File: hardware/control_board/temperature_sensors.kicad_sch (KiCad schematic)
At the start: 23 parts, among them J5 RTD, J5 TC, U2 MAX6675, U6 MCP6N11T-005E, U7 MCP6001T

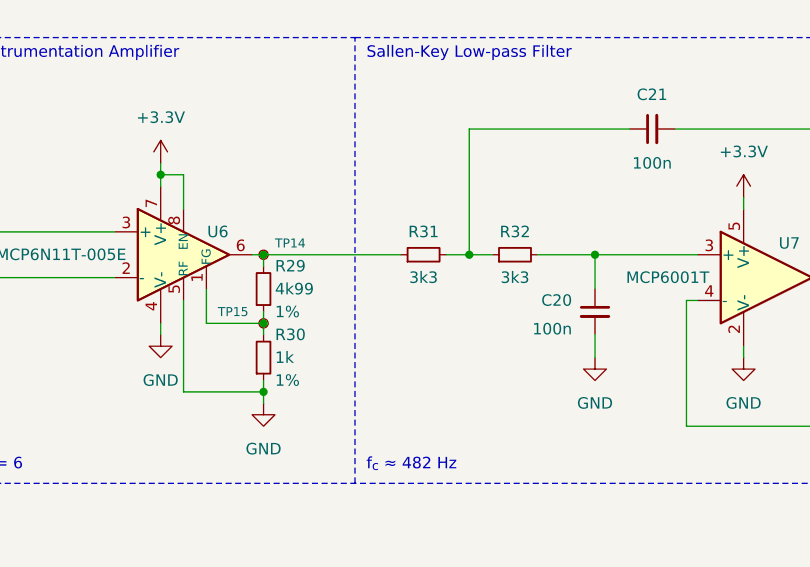
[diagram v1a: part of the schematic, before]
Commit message: Change the buzzer
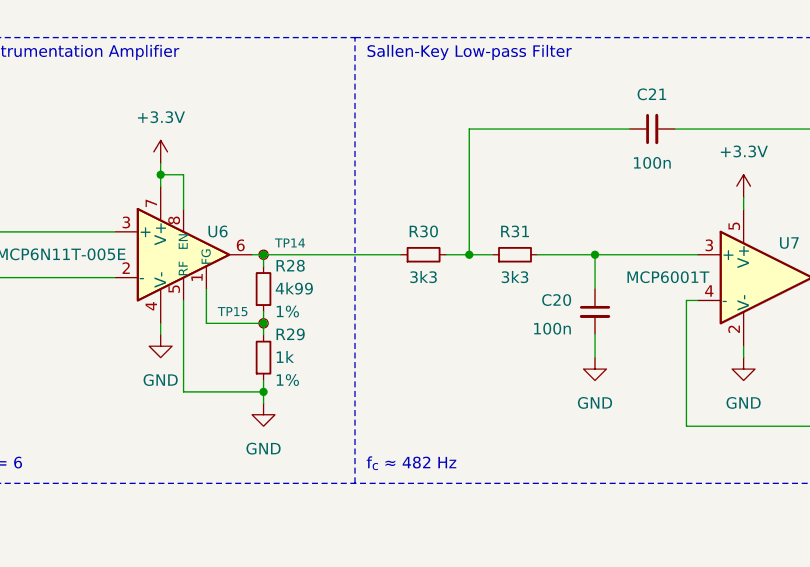
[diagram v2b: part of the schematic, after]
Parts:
- renumbered R29 to R28, R30 to R29, R31 to R30, R32 to R31
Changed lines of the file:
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@@
       (project "control_board"
         (path "/b652b05a-4e3d-4ad1-b032-18886abe7d45/02711725-e382-48ba-bf33-23fe46c66e66"
-          (reference "R28") (unit 1)
+          (reference "R27") (unit 1)
         )
       )
@@
       (project "control_board"
         (path "/b652b05a-4e3d-4ad1-b032-18886abe7d45/02711725-e382-48ba-bf33-23fe46c66e66"
-          (reference "R26") (unit 1)
+          (reference "R25") (unit 1)
         )
       )
@@
       (project "control_board"
         (path "/b652b05a-4e3d-4ad1-b032-18886abe7d45/02711725-e382-48ba-bf33-23fe46c66e66"
-          (reference "R27") (unit 1)
+          (reference "R26") (unit 1)
         )
       )
@@
   (symbol (lib_id "Device:R_Small") (at 146.05 62.23 0) (mirror x) (unit 1)
     (in_bom yes) (on_board yes) (dnp no)
-    (property "Reference" "R29" (at 147.32 59.69 0)
+    (property "Reference" "R28" (at 147.32 59.69 0)
       (effects (font (size 1.27 1.27)) (justify left))
     )
@@
       (project "control_board"
         (path "/b652b05a-4e3d-4ad1-b032-18886abe7d45/02711725-e382-48ba-bf33-23fe46c66e66"
-          (reference "R29") (unit 1)
+          (reference "R28") (unit 1)
         )
       )
@@
   (symbol (lib_id "Device:R_Small") (at 173.99 58.42 90) (unit 1)
     (in_bom yes) (on_board yes) (dnp no)
-    (property "Reference" "R32" (at 173.99 55.88 90)
+    (property "Reference" "R31" (at 173.99 55.88 90)
       (effects (font (size 1.27 1.27)))
     )
@@
       (project "control_board"
         (path "/b652b05a-4e3d-4ad1-b032-18886abe7d45/02711725-e382-48ba-bf33-23fe46c66e66"
-          (reference "R32") (unit 1)
+          (reference "R31") (unit 1)
         )
       )
@@
   (symbol (lib_id "Device:R_Small") (at 146.05 69.85 0) (mirror x) (unit 1)
     (in_bom yes) (on_board yes) (dnp no)
-    (property "Reference" "R30" (at 147.32 67.31 0)
+    (property "Reference" "R29" (at 147.32 67.31 0)
       (effects (font (size 1.27 1.27)) (justify left))
     )
@@
       (project "control_board"
         (path "/b652b05a-4e3d-4ad1-b032-18886abe7d45/02711725-e382-48ba-bf33-23fe46c66e66"
+          (reference "R29") (unit 1)
+        )
+      )
+      (project "apps"
+        (path "/fc4ad874-c922-4070-89f9-7262080469d8/00000000-0000-0000-0000-00006068dc5c"
+          (reference "R?") (unit 1)
+        )
+      )
+    )
+  )
+  (symbol (lib_id "Device:R_Small") (at 163.83 58.42 90) (unit 1)
+    (in_bom yes) (on_board yes) (dnp no)
+    (property "Reference" "R30" (at 163.83 55.88 90)
+      (effects (font (size 1.27 1.27)))
+    )
+    (property "Value" "3k3" (at 163.83 60.96 90)
+      (effects (font (size 1.27 1.27)))
+    )
+    (property "Footprint" "Resistor_SMD:R_0603_1608Metric" (at 163.83 58.42 0)
+      (effects (font (size 1.27 1.27)) hide)
+    )
+    (property "Datasheet" "~" (at 163.83 58.42 0)
+      (effects (font (size 1.27 1.27)) hide)
+    )
+    (pin "1")
+    (pin "2")
+    (instances
+      (project "control_board"
+        (path "/b652b05a-4e3d-4ad1-b032-18886abe7d45/02711725-e382-48ba-bf33-23fe46c66e66"
           (reference "R30") (unit 1)
         )
       )
-      (project "apps"
-        (path "/fc4ad874-c922-4070-89f9-7262080469d8/00000000-0000-0000-0000-00006068dc5c"
-          (reference "R?") (unit 1)
-        )
-      )
-    )
-  )
-  (symbol (lib_id "Device:R_Small") (at 163.83 58.42 90) (unit 1)
-    (in_bom yes) (on_board yes) (dnp no)
-    (property "Reference" "R31" (at 163.83 55.88 90)
-      (effects (font (size 1.27 1.27)))
-    )
-    (property "Value" "3k3" (at 163.83 60.96 90)
-      (effects (font (size 1.27 1.27)))
-    )
-    (property "Footprint" "Resistor_SMD:R_0603_1608Metric" (at 163.83 58.42 0)
-      (effects (font (size 1.27 1.27)) hide)
-    )
-    (property "Datasheet" "~" (at 163.83 58.42 0)
-      (effects (font (size 1.27 1.27)) hide)
-    )
-    (pin "1")
-    (pin "2")
-    (instances
-      (project "control_board"
-        (path "/b652b05a-4e3d-4ad1-b032-18886abe7d45/02711725-e382-48ba-bf33-23fe46c66e66"
-          (reference "R31") (unit 1)
-        )
-      )

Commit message: Add USB D+ pull-up resistor
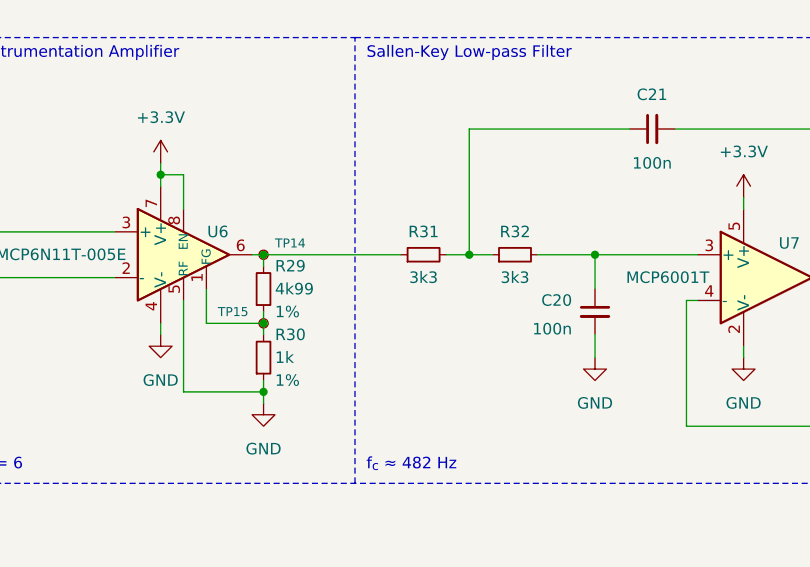
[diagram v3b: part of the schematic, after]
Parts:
- renumbered R28 to R29, R29 to R30, R30 to R31, R31 to R32
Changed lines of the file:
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@@
         )
         (path "/b652b05a-4e3d-4ad1-b032-18886abe7d45/02711725-e382-48ba-bf33-23fe46c66e66"
-          (reference "#PWR064") (unit 1)
+          (reference "#PWR065") (unit 1)
         )
         (path "/b652b05a-4e3d-4ad1-b032-18886abe7d45/d341d3a2-ea4e-4772-851c-7c5b5be32855"
@@
   (symbol (lib_id "power:GND") (at 182.88 69.85 0) (unit 1)
     (in_bom yes) (on_board yes) (dnp no)
-    (property "Reference" "#PWR071" (at 182.88 76.2 0)
+    (property "Reference" "#PWR072" (at 182.88 76.2 0)
       (effects (font (size 1.27 1.27)) hide)
     )
@@
       (project "control_board"
         (path "/b652b05a-4e3d-4ad1-b032-18886abe7d45/02711725-e382-48ba-bf33-23fe46c66e66"
-          (reference "#PWR071") (unit 1)
+          (reference "#PWR072") (unit 1)
         )
       )
@@
       (project "control_board"
         (path "/b652b05a-4e3d-4ad1-b032-18886abe7d45/02711725-e382-48ba-bf33-23fe46c66e66"
-          (reference "R27") (unit 1)
+          (reference "R28") (unit 1)
         )
       )
@@
       (project "control_board"
         (path "/b652b05a-4e3d-4ad1-b032-18886abe7d45/02711725-e382-48ba-bf33-23fe46c66e66"
-          (reference "R25") (unit 1)
+          (reference "R26") (unit 1)
         )
       )
@@
         )
         (path "/b652b05a-4e3d-4ad1-b032-18886abe7d45/02711725-e382-48ba-bf33-23fe46c66e66"
-          (reference "#PWR063") (unit 1)
+          (reference "#PWR064") (unit 1)
         )
       )
@@
         )
         (path "/b652b05a-4e3d-4ad1-b032-18886abe7d45/02711725-e382-48ba-bf33-23fe46c66e66"
-          (reference "#PWR070") (unit 1)
+          (reference "#PWR071") (unit 1)
         )
         (path "/b652b05a-4e3d-4ad1-b032-18886abe7d45/d341d3a2-ea4e-4772-851c-7c5b5be32855"
@@
         )
         (path "/b652b05a-4e3d-4ad1-b032-18886abe7d45/02711725-e382-48ba-bf33-23fe46c66e66"
-          (reference "#PWR066") (unit 1)
+          (reference "#PWR067") (unit 1)
         )
       )
@@
         )
         (path "/b652b05a-4e3d-4ad1-b032-18886abe7d45/02711725-e382-48ba-bf33-23fe46c66e66"
-          (reference "#PWR062") (unit 1)
+          (reference "#PWR063") (unit 1)
         )
       )
@@
         )
         (path "/b652b05a-4e3d-4ad1-b032-18886abe7d45/02711725-e382-48ba-bf33-23fe46c66e66"
-          (reference "#PWR074") (unit 1)
+          (reference "#PWR075") (unit 1)
         )
       )
@@
   (symbol (lib_id "power:GND") (at 146.05 74.93 0) (unit 1)
     (in_bom yes) (on_board yes) (dnp no)
-    (property "Reference" "#PWR068" (at 146.05 81.28 0)
+    (property "Reference" "#PWR069" (at 146.05 81.28 0)
       (effects (font (size 1.27 1.27)) hide)
     )
@@
       (project "control_board"
         (path "/b652b05a-4e3d-4ad1-b032-18886abe7d45/02711725-e382-48ba-bf33-23fe46c66e66"
-          (reference "#PWR068") (unit 1)
+          (reference "#PWR069") (unit 1)
         )
       )
@@
       (project "control_board"
         (path "/b652b05a-4e3d-4ad1-b032-18886abe7d45/02711725-e382-48ba-bf33-23fe46c66e66"
-          (reference "R26") (unit 1)
+          (reference "R27") (unit 1)
         )
       )
@@
   (symbol (lib_id "power:GND") (at 134.62 67.31 0) (unit 1)
     (in_bom yes) (on_board yes) (dnp no)
-    (property "Reference" "#PWR067" (at 134.62 73.66 0)
+    (property "Reference" "#PWR068" (at 134.62 73.66 0)
       (effects (font (size 1.27 1.27)) hide)
     )
@@
       (project "control_board"
         (path "/b652b05a-4e3d-4ad1-b032-18886abe7d45/02711725-e382-48ba-bf33-23fe46c66e66"
-          (reference "#PWR067") (unit 1)
+          (reference "#PWR068") (unit 1)
         )
       )
@@
         )
         (path "/b652b05a-4e3d-4ad1-b032-18886abe7d45/02711725-e382-48ba-bf33-23fe46c66e66"
-          (reference "#PWR065") (unit 1)
+          (reference "#PWR066") (unit 1)
         )
         (path "/b652b05a-4e3d-4ad1-b032-18886abe7d45/d341d3a2-ea4e-4772-851c-7c5b5be32855"
@@
   (symbol (lib_id "Device:R_Small") (at 146.05 62.23 0) (mirror x) (unit 1)
     (in_bom yes) (on_board yes) (dnp no)
-    (property "Reference" "R28" (at 147.32 59.69 0)
+    (property "Reference" "R29" (at 147.32 59.69 0)
       (effects (font (size 1.27 1.27)) (justify left))
     )
@@
       (project "control_board"
         (path "/b652b05a-4e3d-4ad1-b032-18886abe7d45/02711725-e382-48ba-bf33-23fe46c66e66"
-          (reference "R28") (unit 1)
+          (reference "R29") (unit 1)
         )
       )
@@
   (symbol (lib_id "Device:R_Small") (at 173.99 58.42 90) (unit 1)
     (in_bom yes) (on_board yes) (dnp no)
-    (property "Reference" "R31" (at 173.99 55.88 90)
+    (property "Reference" "R32" (at 173.99 55.88 90)
       (effects (font (size 1.27 1.27)))
     )
@@
       (project "control_board"
         (path "/b652b05a-4e3d-4ad1-b032-18886abe7d45/02711725-e382-48ba-bf33-23fe46c66e66"
-          (reference "R31") (unit 1)
+          (reference "R32") (unit 1)
         )
       )
@@
         )
         (path "/b652b05a-4e3d-4ad1-b032-18886abe7d45/02711725-e382-48ba-bf33-23fe46c66e66"
-          (reference "#PWR069") (unit 1)
+          (reference "#PWR070") (unit 1)
         )
       )
@@
   (symbol (lib_id "Device:R_Small") (at 146.05 69.85 0) (mirror x) (unit 1)
     (in_bom yes) (on_board yes) (dnp no)
-    (property "Reference" "R29" (at 147.32 67.31 0)
+    (property "Reference" "R30" (at 147.32 67.31 0)
       (effects (font (size 1.27 1.27)) (justify left))
     )
@@
       (project "control_board"
         (path "/b652b05a-4e3d-4ad1-b032-18886abe7d45/02711725-e382-48ba-bf33-23fe46c66e66"
-          (reference "R29") (unit 1)
+          (reference "R30") (unit 1)
         )
       )
@@
   (symbol (lib_id "Device:R_Small") (at 163.83 58.42 90) (unit 1)
     (in_bom yes) (on_board yes) (dnp no)
-    (property "Reference" "R30" (at 163.83 55.88 90)
+    (property "Reference" "R31" (at 163.83 55.88 90)
       (effects (font (size 1.27 1.27)))
     )
@@
       (project "control_board"
         (path "/b652b05a-4e3d-4ad1-b032-18886abe7d45/02711725-e382-48ba-bf33-23fe46c66e66"
-          (reference "R30") (unit 1)
+          (reference "R31") (unit 1)
         )
       )
@@
   (symbol (lib_id "power:GND") (at 199.39 69.85 0) (unit 1)
     (in_bom yes) (on_board yes) (dnp no)
-    (property "Reference" "#PWR073" (at 199.39 76.2 0)
+    (property "Reference" "#PWR074" (at 199.39 76.2 0)
       (effects (font (size 1.27 1.27)) hide)
     )
@@
       (project "control_board"
         (path "/b652b05a-4e3d-4ad1-b032-18886abe7d45/02711725-e382-48ba-bf33-23fe46c66e66"
-          (reference "#PWR073") (unit 1)
+          (reference "#PWR074") (unit 1)
         )
       )
@@
         )
         (path "/b652b05a-4e3d-4ad1-b032-18886abe7d45/02711725-e382-48ba-bf33-23fe46c66e66"
-          (reference "#PWR072") (unit 1)
+          (reference "#PWR073") (unit 1)
         )
       )
@@
       (project "control_board"
         (path "/b652b05a-4e3d-4ad1-b032-18886abe7d45/02711725-e382-48ba-bf33-23fe46c66e66"
-          (reference "#PWR061") (unit 1)
+          (reference "#PWR062") (unit 1)
         )
       )
@@
   (symbol (lib_id "power:GND") (at 241.3 66.04 0) (unit 1)
     (in_bom yes) (on_board yes) (dnp no)
-    (property "Reference" "#PWR075" (at 241.3 72.39 0)
+    (property "Reference" "#PWR076" (at 241.3 72.39 0)
       (effects (font (size 1.27 1.27)) hide)
     )
@@
       (project "control_board"
         (path "/b652b05a-4e3d-4ad1-b032-18886abe7d45/02711725-e382-48ba-bf33-23fe46c66e66"
-          (reference "#PWR075") (unit 1)
-        )
-      )
+          (reference "#PWR076") (unit 1)
+        )
+      )
